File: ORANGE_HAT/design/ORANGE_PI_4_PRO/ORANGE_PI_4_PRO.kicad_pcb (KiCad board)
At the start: 2 copper layers, 58 x 26 mm, 2 parts, among them P1 Conn_02x20_Odd_Even, P2 Conn_02x20_Odd_Even

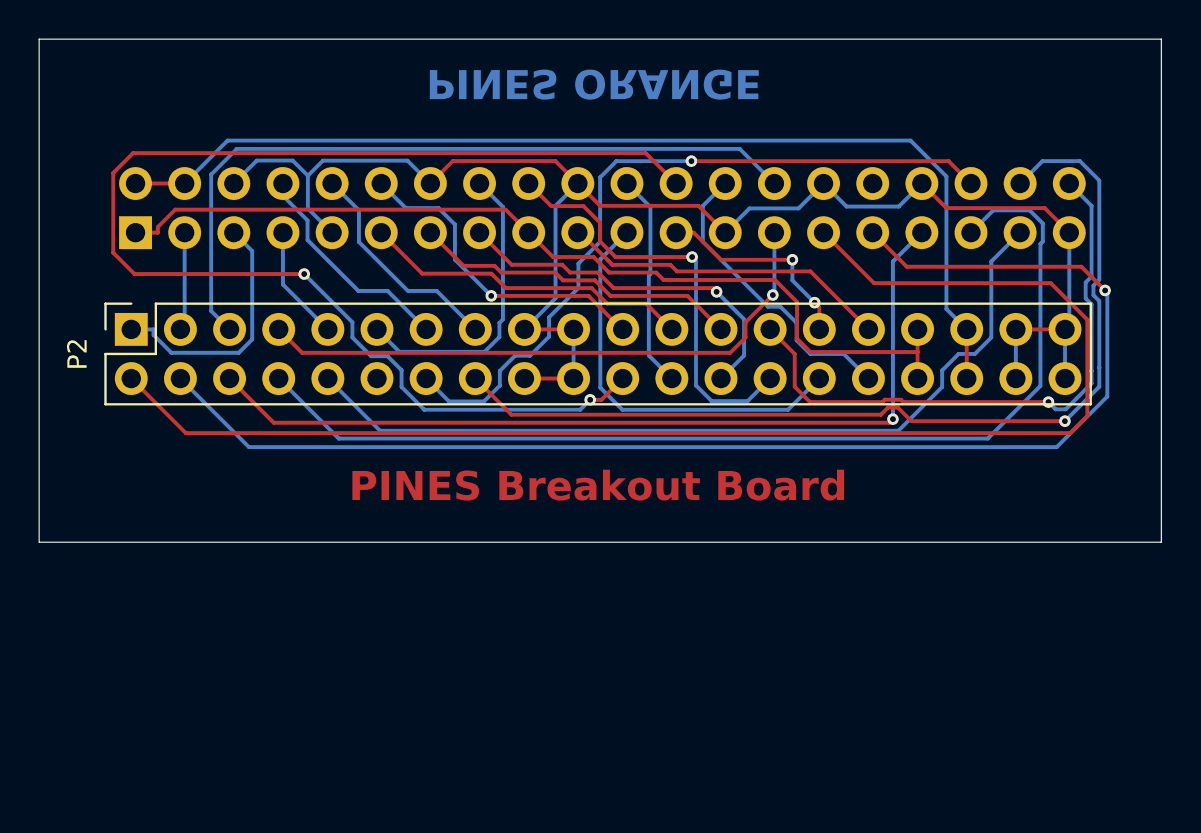
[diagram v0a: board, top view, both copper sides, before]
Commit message: feat: Add Mounting holes
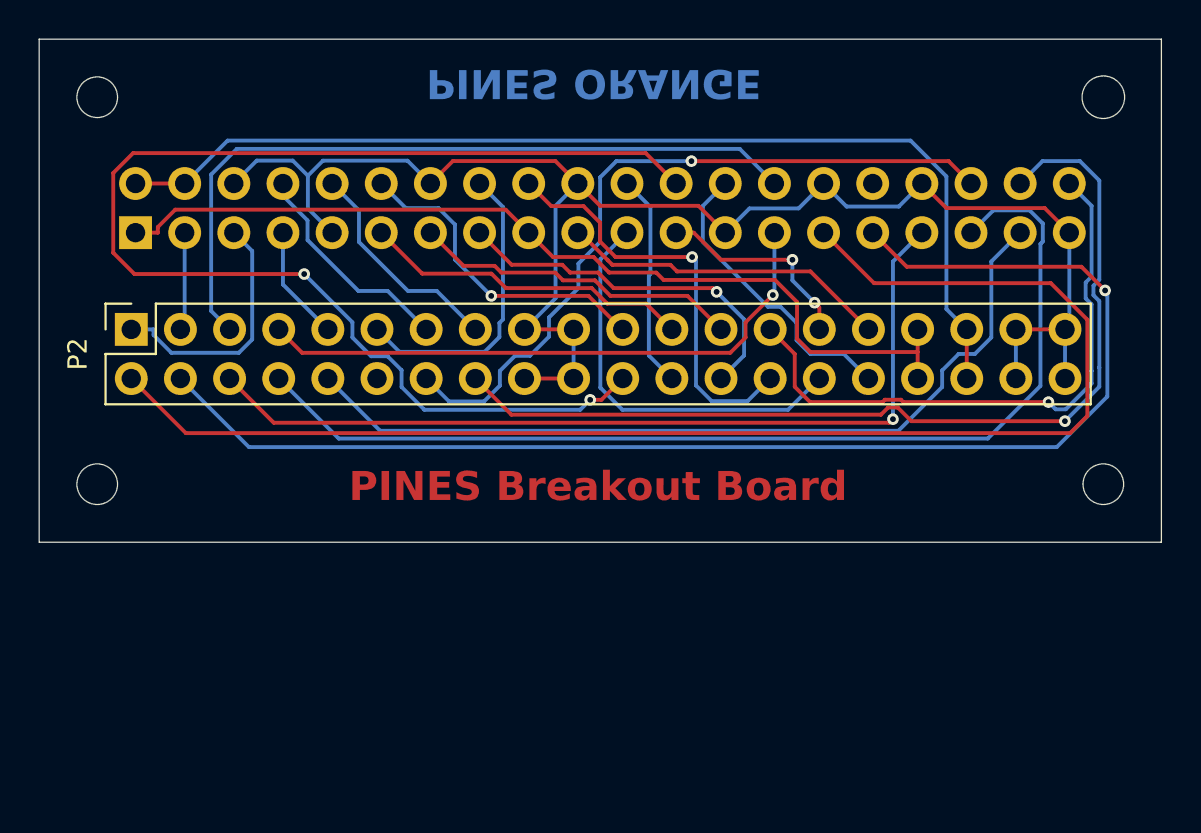
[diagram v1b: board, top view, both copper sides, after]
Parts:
- added REF**: MountingHole_2.1mm, MountingHole:MountingHole_2.1mm, F.Cu at (207.0, 94.0)
- added REF**: MountingHole_2.1mm, MountingHole:MountingHole_2.1mm, F.Cu at (207.0, 114.0)
- added REF**: MountingHole_2.1mm, MountingHole:MountingHole_2.1mm, F.Cu at (259.0, 114.0)
- added REF**: MountingHole_2.2mm_M2, MountingHole:MountingHole_2.2mm_M2, F.Cu at (259.0, 94.0)

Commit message: feat: Git ignore
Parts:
- moved P2 0.24 mm to (209.0, 106.0)
- renumbered REF** to H1, REF** to H2, REF** to H3, REF** to H4
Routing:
- net GND: track 82.4 -> 0.00 mm
- net /PD0: track 71.4 -> 0.00 mm
- net /PD1: track 69.2 -> 0.00 mm, vias 1 -> 0
- net /PE12: track 65.6 -> 0.00 mm, vias 2 -> 0
- net /PD3: track 54.7 -> 0.00 mm
- net +5V: track 54.5 -> 0.00 mm
- net /PD7: track 50.1 -> 0.00 mm, vias 1 -> 0
- net +3.3V: track 47.8 -> 0.00 mm
- net /PD2: track 45.6 -> 0.00 mm, vias 1 -> 0
- net /PD4: track 43.9 -> 0.00 mm
- net /PB4: track 38.8 -> 0.00 mm
- net /PD6: track 38.0 -> 0.00 mm, vias 1 -> 0
- net /PL13: track 31.0 -> 0.00 mm, vias 1 -> 0
- net /PB5: track 31.0 -> 0.00 mm, vias 1 -> 0
- net /PK25: track 22.0 -> 0.00 mm, vias 1 -> 0
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
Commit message: VIAS
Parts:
- added P3: Conn_02x20_Odd_Even, Connector_PinSocket_2.54mm:PinSocket_2x20_P2.54mm_Vertical, F.Cu at (209.0, 119.0)
- moved H3 13.0 mm to (207.0, 127.0)
- moved H4 13.0 mm to (259.0, 127.0)
- moved P1 10.0 mm to (209.0, 111.0)
- moved P2 7.27 mm to (209.0, 98.7)
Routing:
- net GND: track 0.00 -> 171.0 mm, vias 0 -> 4
- net +3.3V: track 0.00 -> 126.0 mm, vias 0 -> 5
- net +5V: track 0.00 -> 95.6 mm, vias 0 -> 2
- net /PD7: track 0.00 -> 86.0 mm, vias 0 -> 1
- net /PD4: track 0.00 -> 69.5 mm, vias 0 -> 2
- net /PE2: track 17.3 -> 73.1 mm, vias 0 -> 4
- net /PD2: track 0.00 -> 53.4 mm, vias 0 -> 1
- net /PD0: track 0.00 -> 53.0 mm, vias 0 -> 2
- net /PL9: track 0.00 -> 43.6 mm, vias 0 -> 2
- net /PL13: track 0.00 -> 43.1 mm, vias 0 -> 1
- net /PD3: track 0.00 -> 42.4 mm, vias 0 -> 1
- net /PD1: track 0.00 -> 41.8 mm
- net /PL12: track 0.00 -> 40.4 mm, vias 0 -> 2
- net /PD6: track 0.00 -> 38.0 mm
- net /PL8: track 0.00 -> 35.9 mm, vias 0 -> 2
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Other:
- board size 58 x 26 mm -> 58 x 39 mm

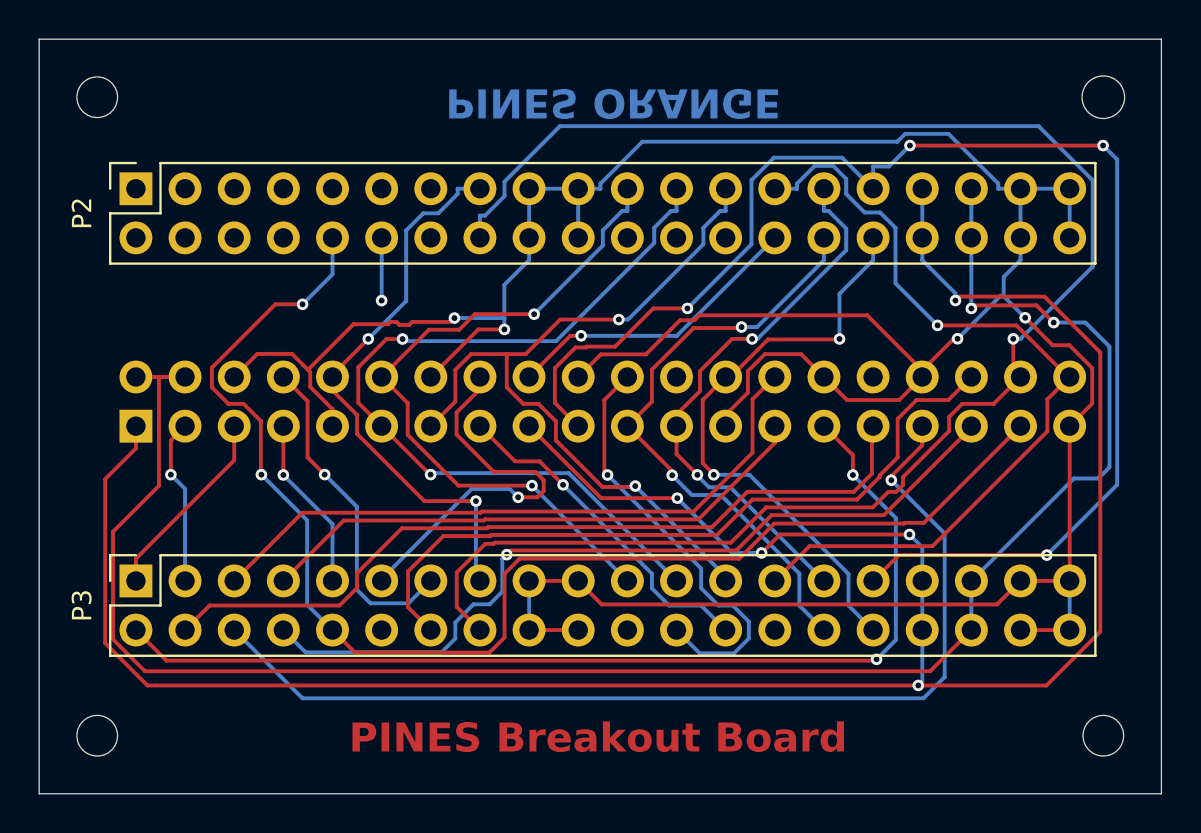
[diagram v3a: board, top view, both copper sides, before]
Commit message: feat: add NO-VIAS zone
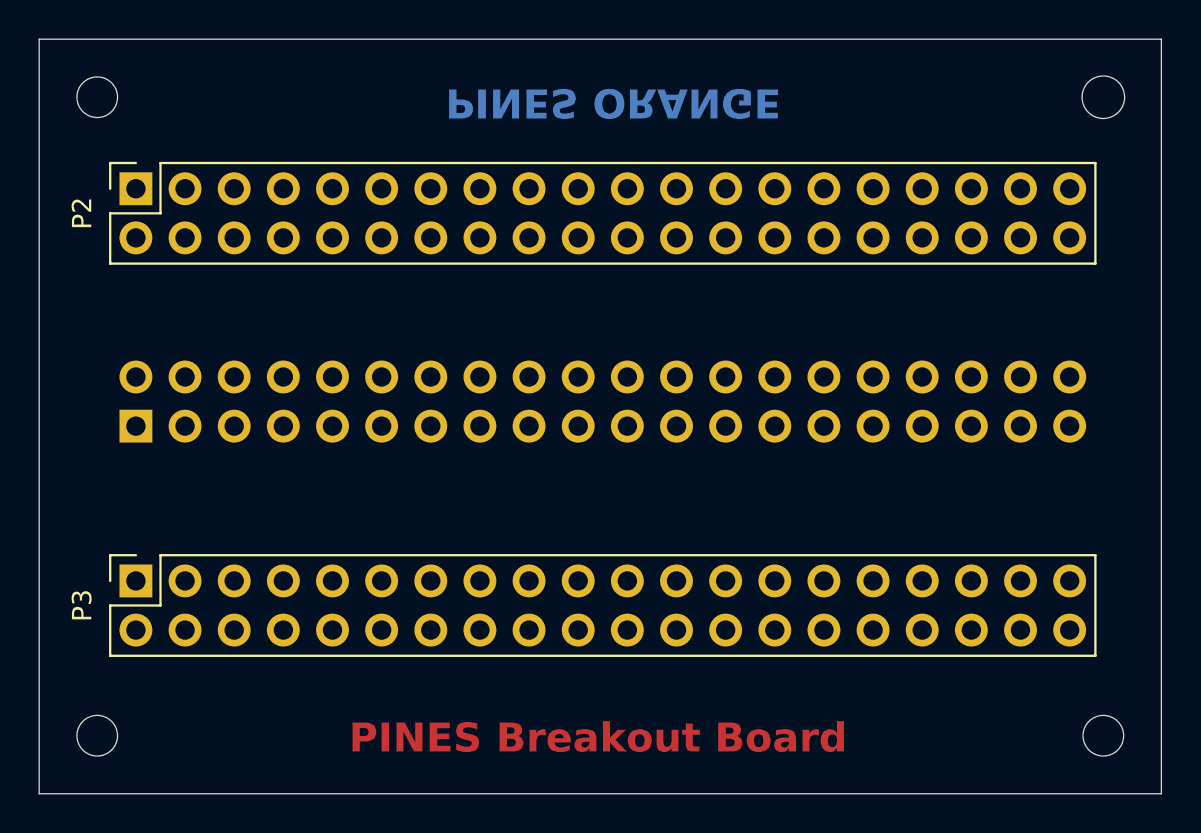
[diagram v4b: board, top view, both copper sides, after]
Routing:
- net GND: track 171.0 -> 0.00 mm, vias 4 -> 0
- net +3.3V: track 126.0 -> 0.00 mm, vias 5 -> 0
- net +5V: track 95.6 -> 0.00 mm, vias 2 -> 0
- net /PD7: track 86.0 -> 0.00 mm, vias 1 -> 0
- net /PE2: track 73.1 -> 0.00 mm, vias 4 -> 0
- net /PD4: track 69.5 -> 0.00 mm, vias 2 -> 0
- net /PD2: track 53.4 -> 0.00 mm, vias 1 -> 0
- net /PD0: track 53.0 -> 0.00 mm, vias 2 -> 0
- net /PL9: track 43.6 -> 0.00 mm, vias 2 -> 0
- net /PL13: track 43.1 -> 0.00 mm, vias 1 -> 0
- net /PD3: track 42.4 -> 0.00 mm, vias 1 -> 0
- net /PD1: track 41.8 -> 0.00 mm
- net /PL12: track 40.4 -> 0.00 mm, vias 2 -> 0
- net /PD6: track 38.0 -> 0.00 mm
- net /PL8: track 35.9 -> 0.00 mm, vias 2 -> 0
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
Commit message: feat: add NO-VIAS zone
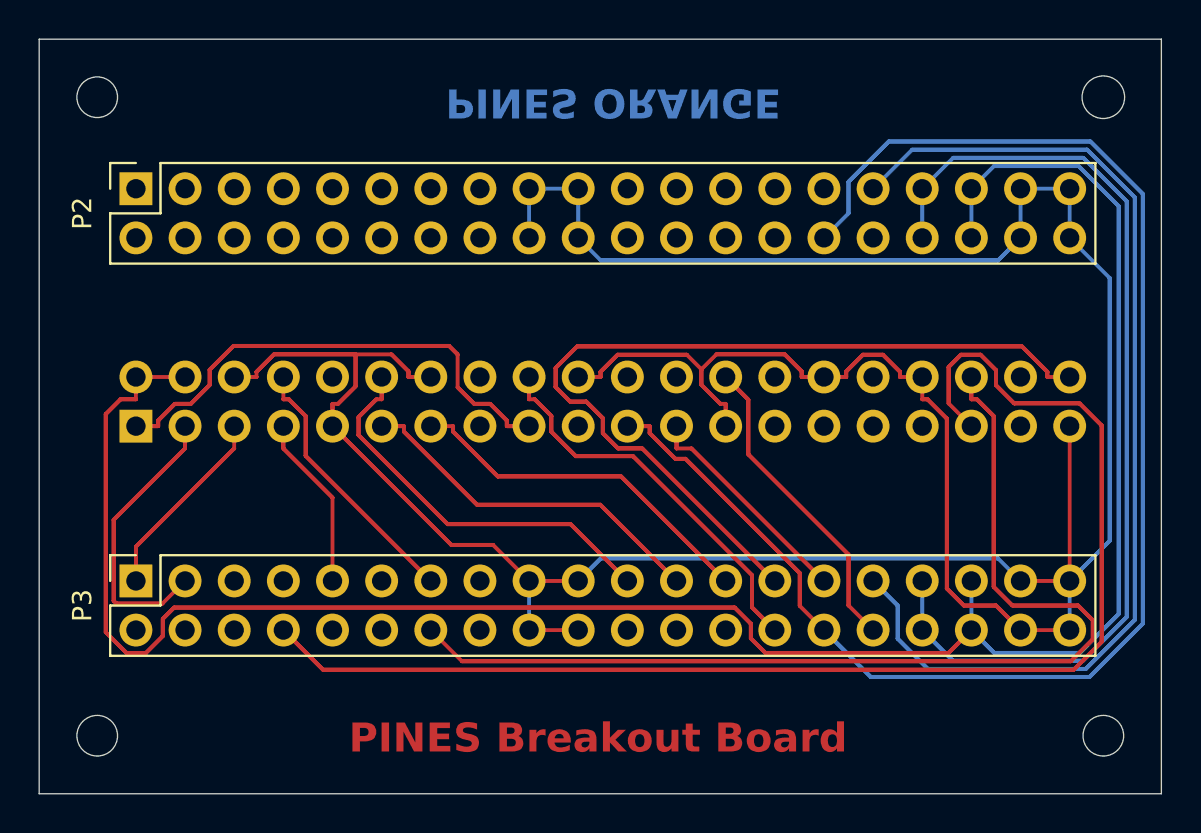
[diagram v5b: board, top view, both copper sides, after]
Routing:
- net GND: track 0.00 -> 297.1 mm
- net +5V: track 0.00 -> 208.5 mm
- net /PE3: track 0.00 -> 150.8 mm
- net +3.3V: track 0.00 -> 143.8 mm
- net /PD3: track 0.00 -> 135.5 mm
- net /PE2: track 0.00 -> 106.5 mm
- net /PD6: track 0.00 -> 105.0 mm
- net /PL13: track 0.00 -> 88.4 mm
- net /PL8: track 0.00 -> 41.1 mm
- net /PK25: track 0.00 -> 40.2 mm
- net /PL9: track 0.00 -> 37.2 mm
- net /PL12: track 0.00 -> 36.3 mm
- net /PE4: track 0.00 -> 30.7 mm
- net /PB3: track 0.00 -> 27.9 mm
- net /PL6: track 0.00 -> 26.6 mm
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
